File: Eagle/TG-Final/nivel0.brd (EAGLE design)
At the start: 21 parts

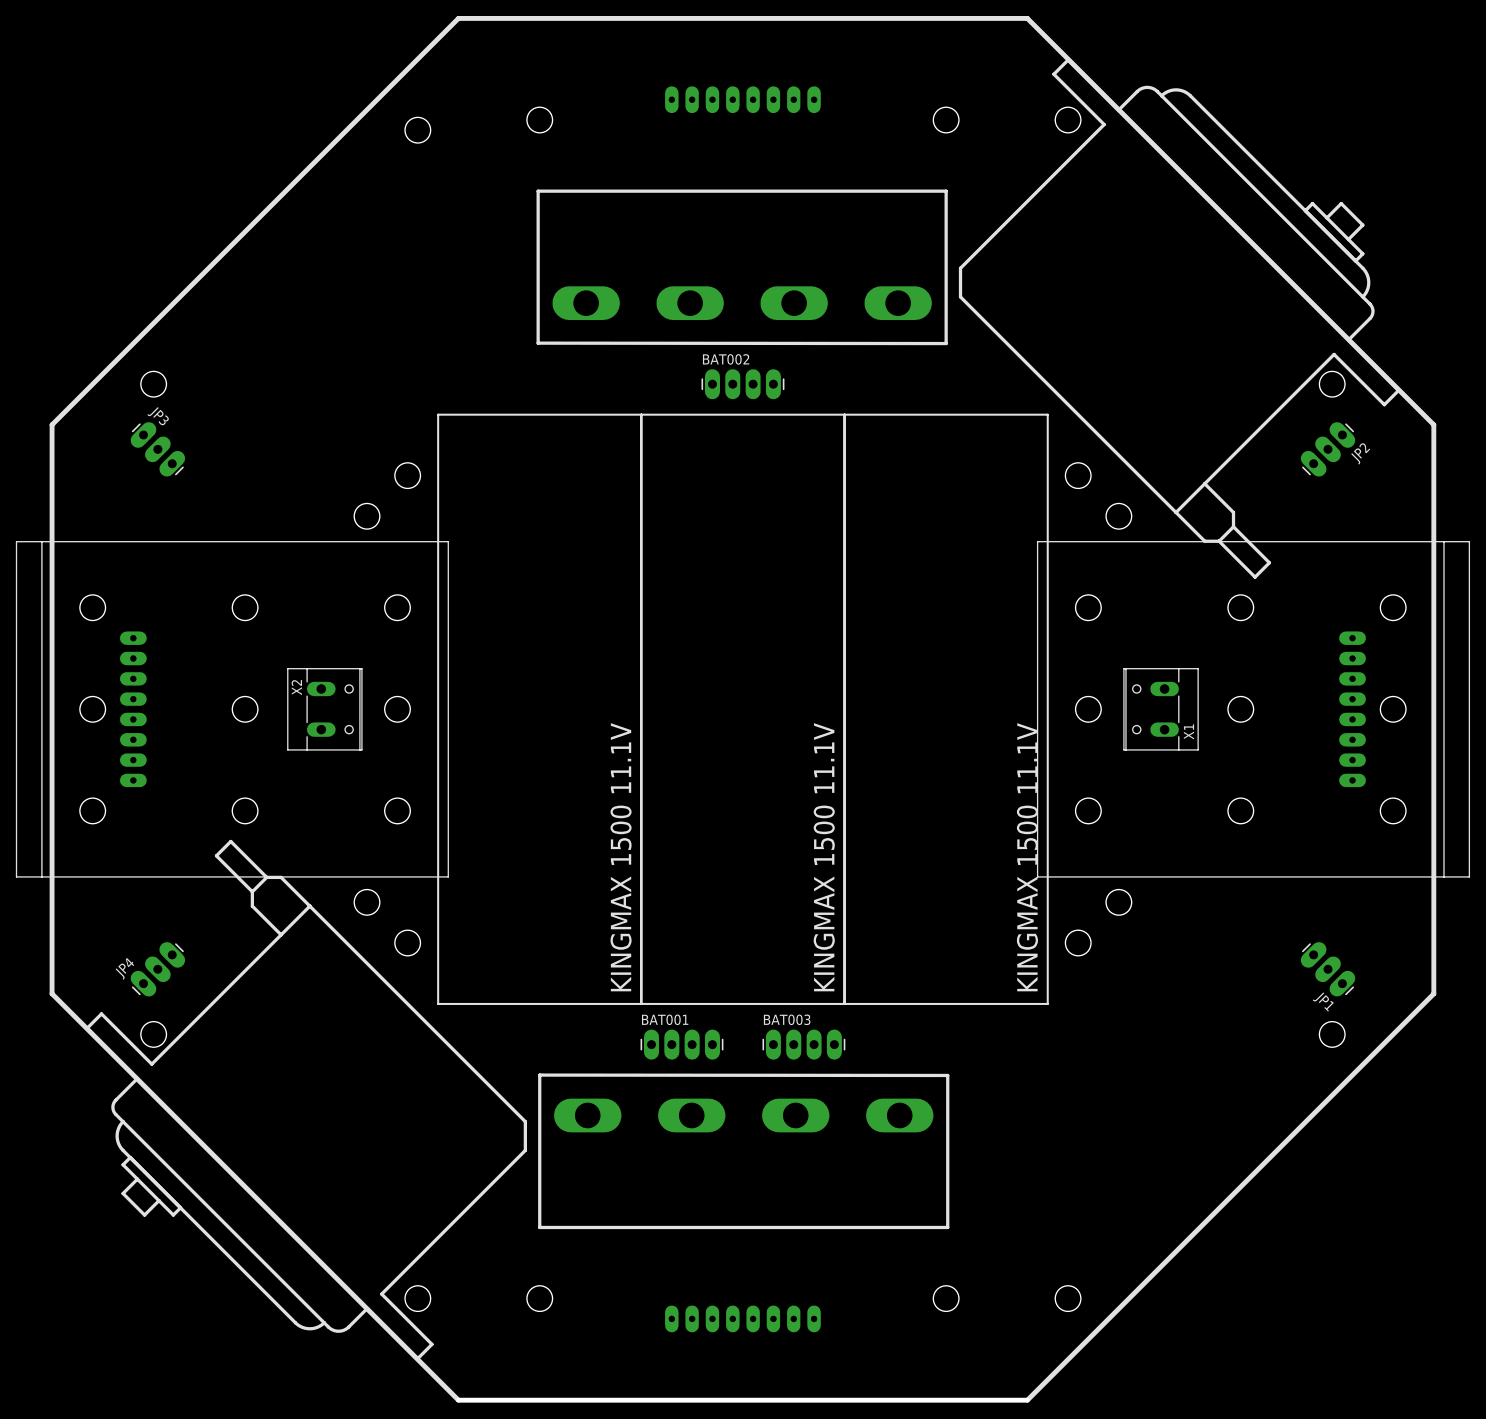
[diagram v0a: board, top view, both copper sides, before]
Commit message: Routing placa Actuadores
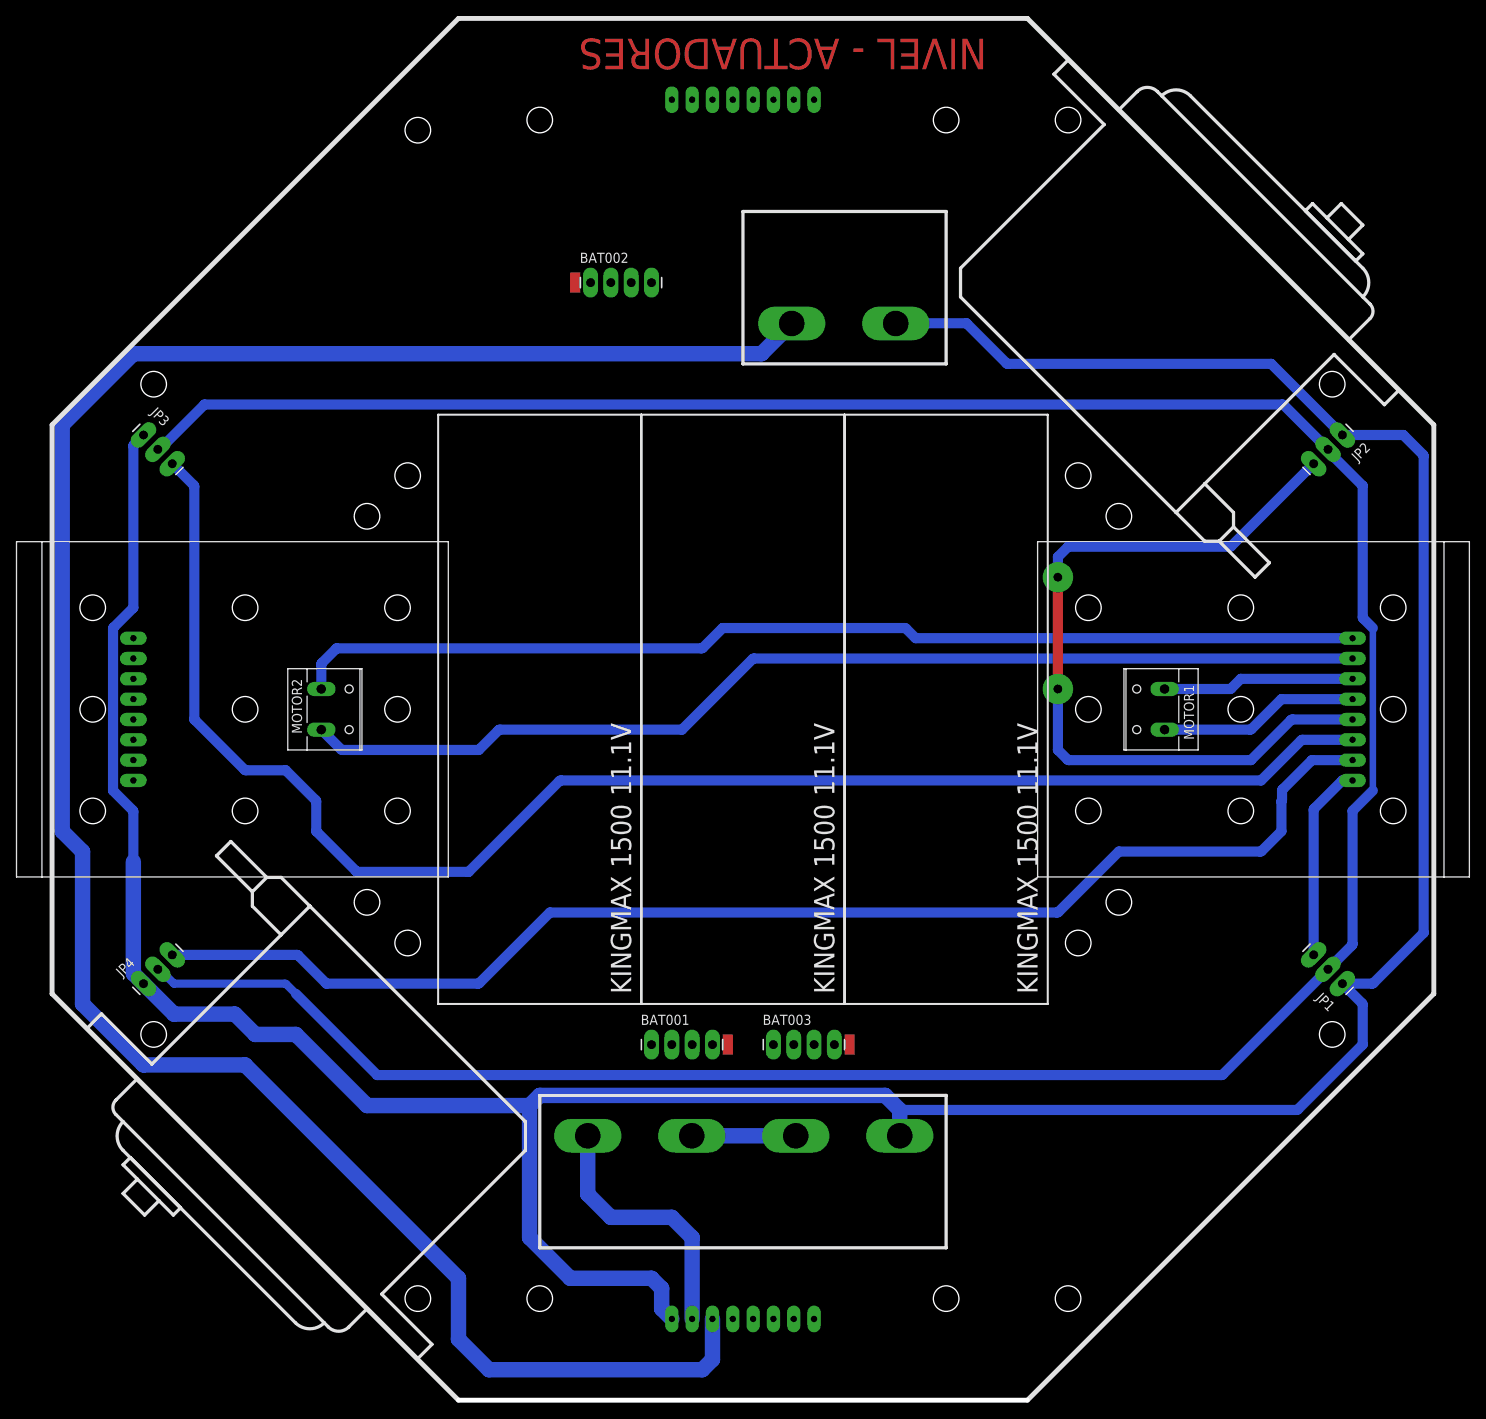
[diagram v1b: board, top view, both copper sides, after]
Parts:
- BAT001, BAT002, BAT003: value (none) -> 11.1v
- JP1, JP2, JP3, JP4, MOTOR1, MOTOR2: value (none) -> (none)
- U$12: value CONECTOR_AUDIO -> CONECTOR_AUDIO2; device aasanchez:CONECTOR_AUDIO -> aasanchez:CONECTOR_AUDIO2
- moved U$11 141.5 mm to (-125.7, 20.3), turned to 0 degrees
- moved U$12 136.8 mm to (-74.9, 149.9), turned to 180 degrees
- moved BAT002 19.8 mm to (-119.4, 141.0)
- renumbered X1 to MOTOR1, X2 to MOTOR2
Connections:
- new net +12V: U$1.PIN18, U$12.P$2
- new net +24V: U$1.PIN17, U$11.P$1
- new net +3V3: U$1.PIN21
- new net +5V: U$1.PIN20
- new net M1-BLACK: MOTOR1.1, U$1.PIN28
- new net M1-RED: MOTOR1.2, U$1.PIN29
- new net M2-BLACK: MOTOR2.1, U$1.PIN31
- new net M2-RED: MOTOR2.2, U$1.PIN30
- new net N$1: U$11.P$2, U$11.P$3
- net SERVO01: now also U$1.PIN24
- net SERVO02: now also U$1.PIN27
- net SERVO03: now also U$1.PIN26
- net SERVO04: now also U$1.PIN25
- net VSS: now also U$1.PIN16, U$11.P$4, U$12.P$1
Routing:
- net VSS: track 0.00 -> 432.2 mm
- net +6V: track 0.00 -> 377.6 mm
- net +12V: track 0.00 -> 277.6 mm
- net SERVO03: track 0.00 -> 194.8 mm
- net SERVO04: track 0.00 -> 163.5 mm
- net M2-RED: track 0.00 -> 134.6 mm
- net M2-BLACK: track 0.00 -> 134.4 mm
- net SERVO02: track 0.00 -> 100.3 mm, vias 0 -> 2
- net +24V: track 0.00 -> 32.8 mm
- net M1-BLACK: track 0.00 -> 25.1 mm
- net SERVO01: track 0.00 -> 24.5 mm
- net M1-RED: track 0.00 -> 24.0 mm
- net N$1: track 0.00 -> 13.0 mm
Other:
- board text added: "NIVEL - ACTUADORES"

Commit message: Routing placa Actuadores. Listo??
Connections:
- removed net +6V: JP1.2, JP2.2, JP3.2, JP4.2
- new net P$1: JP1.2, JP2.2, JP3.2, JP4.2, U$1.PIN19
- new net SENSE1: BAT001.1, U$1.PIN15
- new net SENSE2: BAT002.4, U$1.PIN13
- new net SENSE3: BAT003.1, U$1.PIN14
- net VSS: now also BAT001.4, BAT002.1, BAT003.4
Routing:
- net P$1: track 0.00 -> 481.1 mm, vias 0 -> 2
- net +6V: track 377.6 -> 0.00 mm
- net SENSE2: track 0.00 -> 279.6 mm, vias 0 -> 4
- net SENSE1: track 0.00 -> 154.6 mm, vias 0 -> 2
- net SENSE3: track 0.00 -> 139.7 mm, vias 0 -> 2
- net VSS: track 432.2 -> 511.0 mm
- net +12V: track 277.6 -> 281.0 mm
- net SERVO04: track 163.5 -> 166.7 mm
- added copper zone on layer 16, net N$2
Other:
- board outline added: 172.7 x 172.7 mm
- board text added: "ARN"
- board text added: "NAVR"
- board text added: "NRA"
- board text added: "RVAN"

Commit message: Mejoras en placa de Actuadores y otros
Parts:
- moved MOTOR2 3.81 mm to (-156.2, 87.6)
- moved MOTOR1 3.81 mm to (-44.5, 87.6)
- moved U$5 1.27 mm to (-161.3, 87.6)
- moved U$6 1.27 mm to (-39.4, 87.6)
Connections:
- net +24V renamed +22V
- removed net P$1: JP1.2, JP2.2, JP3.2, JP4.2, U$1.PIN19
- new net +11V1: U$1.PIN19, U$12.P$2
- new net +6V: JP1.2, JP2.2, JP3.2, JP4.2, U$1.PIN20
- net +12V: no longer U$12.P$2
- net +3V3: now also U$1.PIN22; no longer U$1.PIN21
- net +5V: now also U$1.PIN21; no longer U$1.PIN20
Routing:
- net P$1: track 481.1 -> 0.00 mm, vias 2 -> 0
- net +6V: track 0.00 -> 447.6 mm, vias 0 -> 2
- net +12V: track 281.0 -> 0.00 mm
- net +11V1: track 0.00 -> 280.7 mm
- net SERVO02: track 100.3 -> 82.8 mm
- net SENSE2: track 279.6 -> 289.4 mm
- net M2-RED: track 134.6 -> 138.7 mm
- net M1-BLACK: track 25.1 -> 21.2 mm
- net M1-RED: track 24.0 -> 20.2 mm
- net M2-BLACK: track 134.4 -> 136.4 mm
- net SENSE1: track 154.6 -> 155.4 mm
- net SENSE3: track 139.7 -> 139.0 mm
- net +22V: track 32.8 -> 32.0 mm

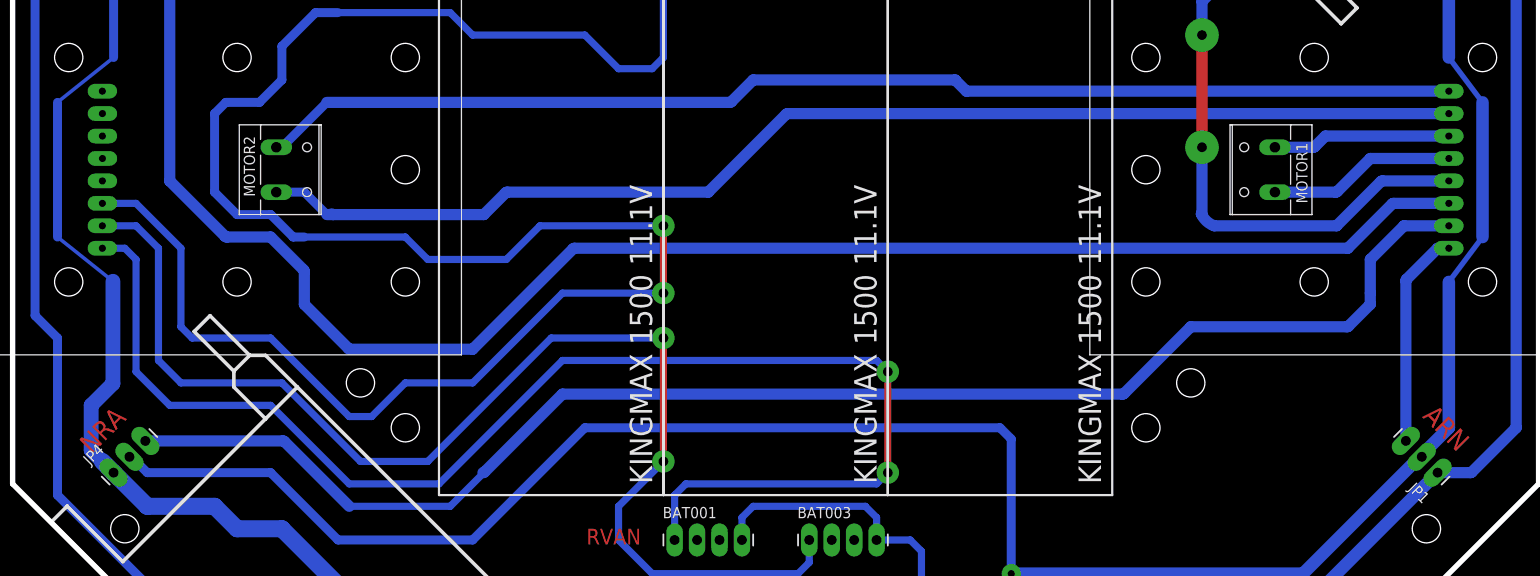
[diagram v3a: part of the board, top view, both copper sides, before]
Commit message: Fuente 11.1v -> 5v y 3v3
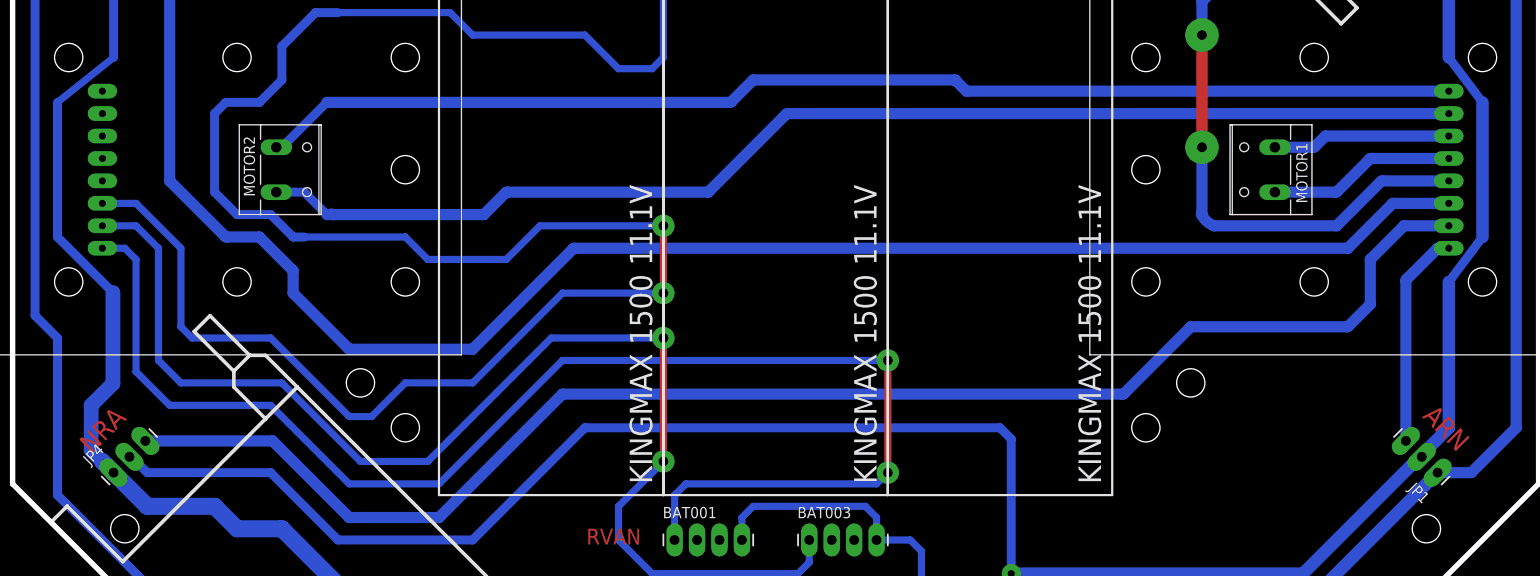
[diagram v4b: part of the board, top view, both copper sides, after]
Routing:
- net SERVO04: track 166.8 -> 167.8 mm
- net SENSE1: track 155.4 -> 156.1 mm
- net SERVO03: track 194.8 -> 194.0 mm

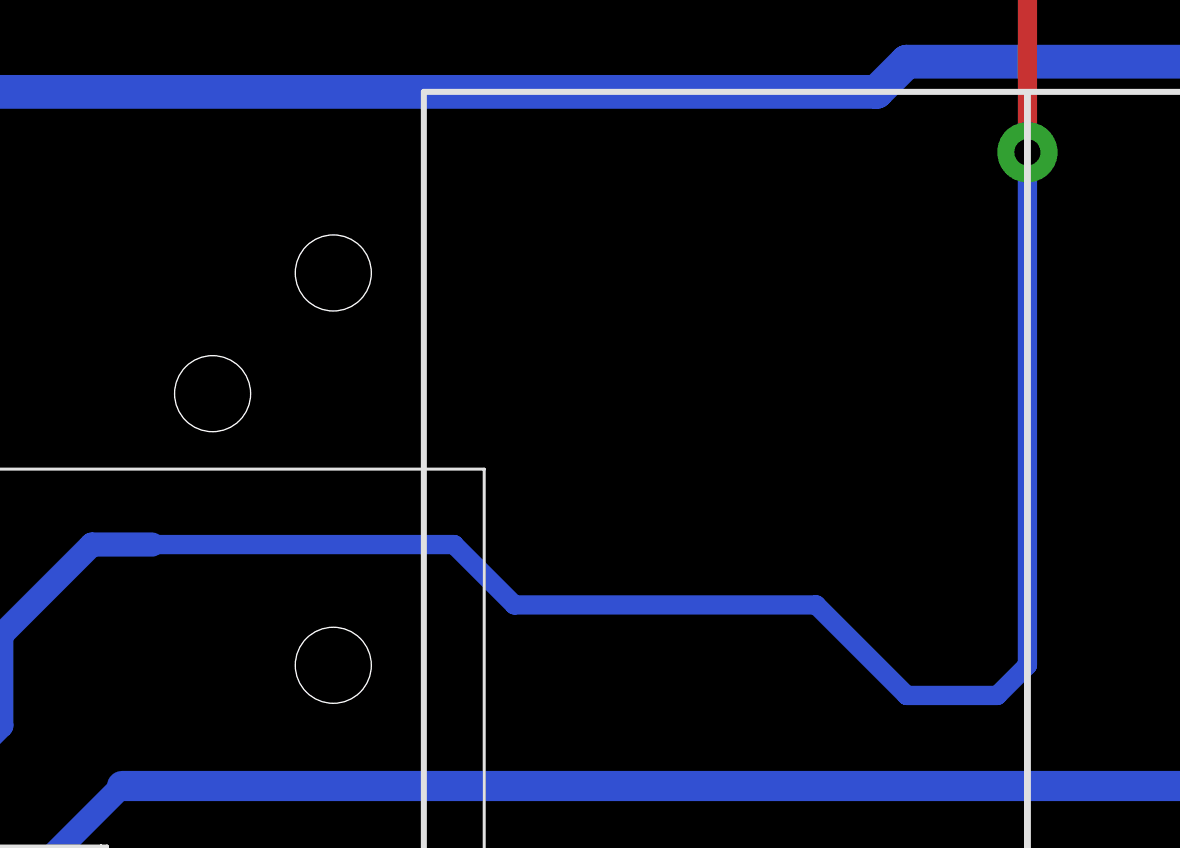
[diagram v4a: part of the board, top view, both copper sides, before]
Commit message: Monitor Baterias LiPO
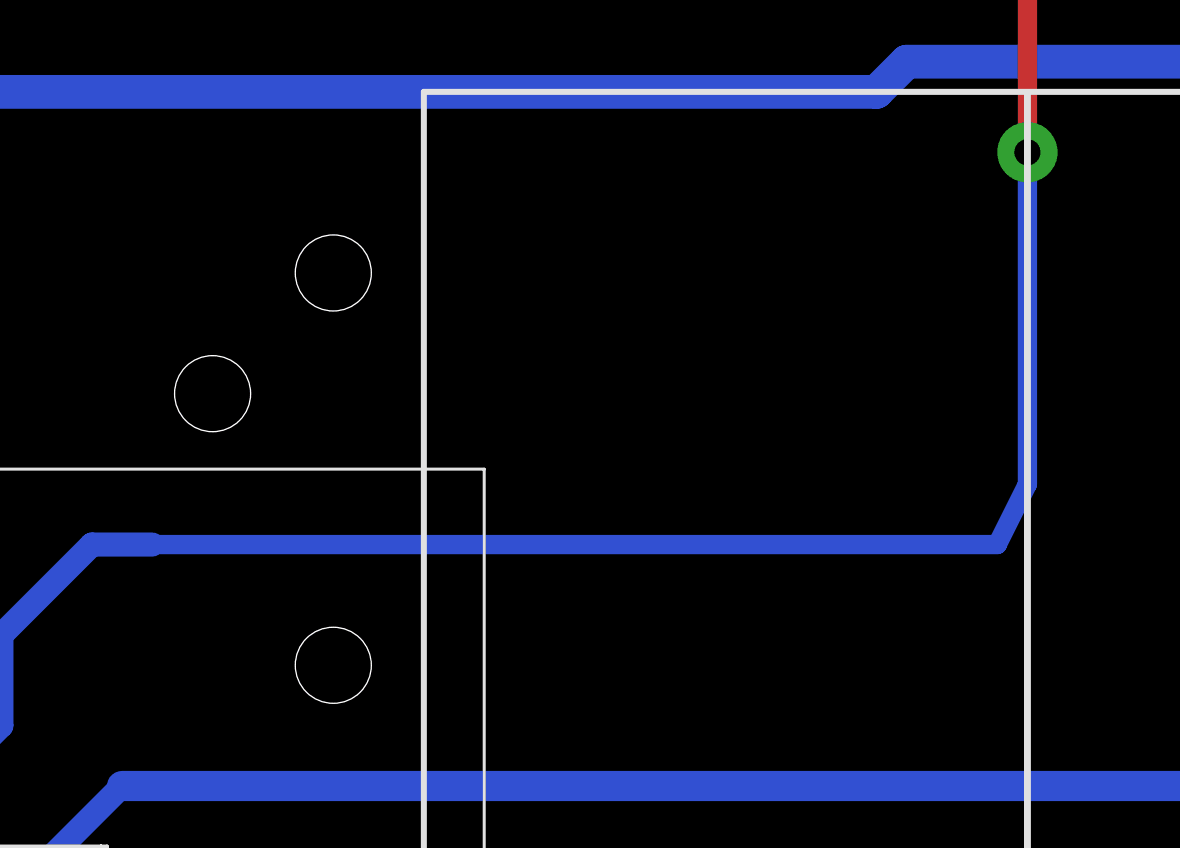
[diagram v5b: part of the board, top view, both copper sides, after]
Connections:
- removed net +12V: U$1.PIN18
- removed net +3V3: U$1.PIN22
- removed net +5V: U$1.PIN21
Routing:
- net SENSE2: track 289.4 -> 280.2 mm
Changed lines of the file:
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@@
 <wire x1="-114.3" y1="133.35" x2="-113.03" y2="132.08" width="0.8128" layer="16"/>
 <wire x1="-113.03" y1="132.08" x2="-113.03" y2="121.92" width="0.8128" layer="1"/>
-<wire x1="-113.03" y1="121.92" x2="-113.03" y2="100.33" width="0.8128" layer="16"/>
-<wire x1="-113.03" y1="100.33" x2="-114.3" y2="99.06" width="0.8128" layer="16"/>
-<wire x1="-114.3" y1="99.06" x2="-118.11" y2="99.06" width="0.8128" layer="16"/>
-<wire x1="-118.11" y1="99.06" x2="-121.92" y2="102.87" width="0.8128" layer="16"/>
-<wire x1="-121.92" y1="102.87" x2="-134.62" y2="102.87" width="0.8128" layer="16"/>
-<wire x1="-134.62" y1="102.87" x2="-137.16" y2="105.41" width="0.8128" layer="16"/>
-<wire x1="-137.16" y1="105.41" x2="-149.86" y2="105.41" width="0.8128" layer="16"/>
+<wire x1="-113.03" y1="121.92" x2="-113.03" y2="107.95" width="0.8128" layer="16"/>
+<wire x1="-113.03" y1="107.95" x2="-114.3" y2="105.41" width="0.8128" layer="16"/>
+<wire x1="-114.3" y1="105.41" x2="-149.86" y2="105.41" width="0.8128" layer="16"/>
 <wire x1="-153.67" y1="80.01" x2="-142.24" y2="80.01" width="0.8128" layer="16"/>
 <wire x1="-142.24" y1="80.01" x2="-139.7" y2="77.47" width="0.8128" layer="16"/>
@@
 <wire x1="-106.68" y1="20.32" x2="-106.68" y2="11.43" width="1.6764" layer="16"/>
 <wire x1="-119.73" y1="34.32" x2="-119.73" y2="27.02" width="1.6764" layer="16"/>
-</signal>
-<signal name="+12V">
-<contactref element="U$1" pad="PIN18"/>
 </signal>
 <signal name="+11V1">
@@
 <wire x1="-73.66" y1="57.15" x2="-73.66" y2="41.91" width="1.016" layer="16"/>
 </signal>
-<signal name="+5V">
-<contactref element="U$1" pad="PIN21"/>
-</signal>
-<signal name="+3V3">
-<contactref element="U$1" pad="PIN22"/>
-</signal>
 <signal name="N$2">

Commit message: Trabajos en la Sub Estacion
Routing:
- net +22V: track 32.0 -> 24.7 mm
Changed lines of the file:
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@@
 <wire x1="-109.22" y1="22.86" x2="-106.68" y2="20.32" width="1.6764" layer="16"/>
 <wire x1="-106.68" y1="20.32" x2="-106.68" y2="11.43" width="1.6764" layer="16"/>
-<wire x1="-119.73" y1="34.32" x2="-119.73" y2="27.02" width="1.6764" layer="16"/>
+<wire x1="-119.73" y1="34.32" x2="-119.73" y2="27.02" width="0" layer="19" extent="1-16"/>
 </signal>
 <signal name="+11V1">
